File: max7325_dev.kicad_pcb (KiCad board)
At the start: 2 copper layers, 0 parts

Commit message: pcb: Place components on PCB
1. Export NET file from schematic editor
2. Import NET file in PCB editor

Signed-off-by: Sam Protsenko <joe.skb7@gmail.com>
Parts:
- added C1: 0.1uF, Capacitors_SMD:C_1206, F.Cu at (111.8, 35.6)
- added D0: LED, LEDs:LED_D5.0mm, F.Cu at (148.6, 83.8)
- added D1: LED, LEDs:LED_D5.0mm, F.Cu at (156.2, 83.8)
- added D10: LED, LEDs:LED_D5.0mm, F.Cu at (163.8, 72.4)
- added D11: LED, LEDs:LED_D5.0mm, F.Cu at (171.4, 72.4)
- added D12: LED, LEDs:LED_D5.0mm, F.Cu at (179.1, 72.4)
- added D13: LED, LEDs:LED_D5.0mm, F.Cu at (186.7, 72.4)
- added D14: LED, LEDs:LED_D5.0mm, F.Cu at (194.3, 72.4)
- added D15: LED, LEDs:LED_D5.0mm, F.Cu at (201.9, 72.4)
- added D2: LED, LEDs:LED_D5.0mm, F.Cu at (163.8, 83.8)
- added D3: LED, LEDs:LED_D5.0mm, F.Cu at (171.4, 83.8)
- added D4: LED, LEDs:LED_D5.0mm, F.Cu at (179.1, 83.8)
- added D5: LED, LEDs:LED_D5.0mm, F.Cu at (186.7, 83.8)
- added D6: LED, LEDs:LED_D5.0mm, F.Cu at (194.3, 83.8)
- added D7: LED, LEDs:LED_D5.0mm, F.Cu at (201.9, 83.8)
- added D8: LED, LEDs:LED_D5.0mm, F.Cu at (148.6, 72.4)
- added D9: LED, LEDs:LED_D5.0mm, F.Cu at (156.2, 72.4)
- added J1: Conn_01x06, Pin_Headers:Pin_Header_Straight_1x06_Pitch2.54mm, F.Cu at (105.4, 47.0)
- added JP0: Jumper_NC_Dual, Pin_Headers:Pin_Header_Straight_1x03_Pitch2.54mm, F.Cu at (179.1, 102.9)
- added JP1: Jumper_NC_Dual, Pin_Headers:Pin_Header_Straight_1x03_Pitch2.54mm, F.Cu at (190.5, 102.9)
- added JP2: Jumper_NC_Dual, Pin_Headers:Pin_Header_Straight_1x03_Pitch2.54mm, F.Cu at (203.2, 102.9)
- added JP3: Jumper_NC_Dual, Pin_Headers:Pin_Header_Straight_1x03_Pitch2.54mm, F.Cu at (215.9, 102.9)
- added JP4: Jumper_NC_Dual, Pin_Headers:Pin_Header_Straight_1x03_Pitch2.54mm, F.Cu at (228.6, 102.9)
- added JP5: Jumper_NC_Dual, Pin_Headers:Pin_Header_Straight_1x03_Pitch2.54mm, F.Cu at (242.6, 102.9)
- added JP6: Jumper_NC_Dual, Pin_Headers:Pin_Header_Straight_1x03_Pitch2.54mm, F.Cu at (256.5, 102.9)
- added JP7: Jumper_NC_Dual, Pin_Headers:Pin_Header_Straight_1x03_Pitch2.54mm, F.Cu at (271.8, 102.9)
- added MK1: Mounting_Hole_PAD, Mounting_Holes:MountingHole_3.2mm_M3_Pad, F.Cu at (115.6, 130.8)
- added MK2: Mounting_Hole_PAD, Mounting_Holes:MountingHole_3.2mm_M3_Pad, F.Cu at (128.3, 130.8)
- added MK3: Mounting_Hole_PAD, Mounting_Holes:MountingHole_3.2mm_M3_Pad, F.Cu at (143.5, 130.8)
- added MK4: Mounting_Hole_PAD, Mounting_Holes:MountingHole_3.2mm_M3_Pad, F.Cu at (158.8, 130.8)
- added R0: 220R, Resistors_SMD:R_1206, F.Cu at (135.9, 76.2)
- added R1: 220R, Resistors_SMD:R_1206, F.Cu at (135.9, 69.8)
- added R10: 220R, Resistors_SMD:R_1206, F.Cu at (128.3, 57.1)
- added R11: 220R, Resistors_SMD:R_1206, F.Cu at (128.3, 50.8)
- added R12: 220R, Resistors_SMD:R_1206, F.Cu at (128.3, 45.7)
- added R13: 220R, Resistors_SMD:R_1206, F.Cu at (128.3, 40.6)
- added R14: 220R, Resistors_SMD:R_1206, F.Cu at (128.3, 35.6)
- added R15: 220R, Resistors_SMD:R_1206, F.Cu at (120.7, 35.6)
- added R16: 10k, Resistors_SMD:R_1206, F.Cu at (120.7, 40.6)
- added R17: 10k, Resistors_SMD:R_1206, F.Cu at (120.7, 45.7)
- added R18: 0R, Resistors_SMD:R_1206, F.Cu at (120.7, 50.8)
- added R19: 0R, Resistors_SMD:R_1206, F.Cu at (120.7, 57.1)
- added R2: 220R, Resistors_SMD:R_1206, F.Cu at (135.9, 63.5)
- added R20: 0R, Resistors_SMD:R_1206, F.Cu at (120.7, 63.5)
- added R21: 0R, Resistors_SMD:R_1206, F.Cu at (120.7, 69.8)
- added R22: 10k, Resistors_SMD:R_1206, F.Cu at (120.7, 76.2)
- added R23: 10k, Resistors_SMD:R_1206, F.Cu at (120.7, 81.3)
- added R24: 10k, Resistors_SMD:R_1206, F.Cu at (120.7, 87.6)
- added R25: 10k, Resistors_SMD:R_1206, F.Cu at (120.7, 94.0)
- added R26: 10k, Resistors_SMD:R_1206, F.Cu at (120.7, 99.1)
- added R27: 10k, Resistors_SMD:R_1206, F.Cu at (120.7, 104.1)
- added R28: 10k, Resistors_SMD:R_1206, F.Cu at (120.7, 109.2)
- added R29: 10k, Resistors_SMD:R_1206, F.Cu at (120.7, 114.3)
- added R3: 220R, Resistors_SMD:R_1206, F.Cu at (135.9, 57.1)
- added R4: 220R, Resistors_SMD:R_1206, F.Cu at (135.9, 50.8)
- added R5: 220R, Resistors_SMD:R_1206, F.Cu at (135.9, 45.7)
- added R6: 220R, Resistors_SMD:R_1206, F.Cu at (135.9, 40.6)
- added R7: 220R, Resistors_SMD:R_1206, F.Cu at (135.9, 35.6)
- added R8: 220R, Resistors_SMD:R_1206, F.Cu at (128.3, 69.8)
- added R9: 220R, Resistors_SMD:R_1206, F.Cu at (128.3, 63.5)
- added SW0: SW_Push, Buttons_Switches_THT:SW_PUSH_6mm, F.Cu at (147.3, 57.1)
- added SW1: SW_Push, Buttons_Switches_THT:SW_PUSH_6mm, F.Cu at (158.8, 57.1)
- added SW2: SW_Push, Buttons_Switches_THT:SW_PUSH_6mm, F.Cu at (170.2, 57.1)
- added SW3: SW_Push, Buttons_Switches_THT:SW_PUSH_6mm, F.Cu at (181.6, 57.1)
- added SW4: SW_Push, Buttons_Switches_THT:SW_PUSH_6mm, F.Cu at (193.0, 57.1)
- added SW5: SW_Push, Buttons_Switches_THT:SW_PUSH_6mm, F.Cu at (204.5, 57.1)
- added SW6: SW_Push, Buttons_Switches_THT:SW_PUSH_6mm, F.Cu at (215.9, 57.1)
- added SW7: SW_Push, Buttons_Switches_THT:SW_PUSH_6mm, F.Cu at (227.3, 57.1)
- added U1: MAX7325AEG+, Housings_SSOP:QSOP-24_3.9x8.7mm_Pitch0.635mm, F.Cu at (105.4, 74.9)

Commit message: pcb: Finish PCB layout
Signed-off-by: Sam Protsenko <joe.skb7@gmail.com>
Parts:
- removed R22, R23, R24, R25, R26, R27, R28, R29: 10k, Resistors_SMD:R_1206
- added R100: 10k, Resistors_SMD:R_1206, B.Cu at (110.5, 80.0)
- added R101: 10k, Resistors_SMD:R_1206, B.Cu at (100.3, 80.0)
- added R102: 10k, Resistors_SMD:R_1206, B.Cu at (90.2, 80.0)
- added R103: 10k, Resistors_SMD:R_1206, B.Cu at (80.0, 80.0)
- added R104: 10k, Resistors_SMD:R_1206, B.Cu at (69.8, 80.0)
- added R105: 10k, Resistors_SMD:R_1206, B.Cu at (59.7, 80.0)
- added R106: 10k, Resistors_SMD:R_1206, B.Cu at (49.5, 80.0)
- added R107: 10k, Resistors_SMD:R_1206, B.Cu at (39.4, 80.0)
- C1, R0, R1, R10, R11, R12, R13, R14, R15, R16, R17, R18, R19, R2, R20, R21, R3, R4, R5, R6, R7, R8, R9, U1: moved to B.Cu
- moved JP7 236.6 mm to (36.8, 74.9), turned to 90 degrees
- moved JP6 211.4 mm to (47.0, 74.9), turned to 90 degrees
- moved SW7 194.0 mm to (36.8, 94.0)
- moved JP5 187.5 mm to (57.1, 74.9), turned to 90 degrees
- moved SW6 172.9 mm to (47.0, 94.0)
- moved JP4 163.7 mm to (67.3, 74.9), turned to 90 degrees
- moved D7 162.6 mm to (39.4, 85.1), turned to 270 degrees
- moved SW5 151.9 mm to (57.1, 94.0)
- moved D6 144.8 mm to (49.5, 85.1), turned to 270 degrees
- moved JP3 141.2 mm to (77.5, 74.9), turned to 90 degrees
- moved MK1 133.3 mm to (29.2, 29.2)
- moved SW4 131.0 mm to (67.3, 94.0)
- moved D5 127.0 mm to (59.7, 85.1), turned to 270 degrees
- moved JP2 118.9 mm to (87.6, 74.9), turned to 90 degrees
- moved MK3 118.0 mm to (29.2, 101.6)
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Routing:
- net +3V3: track 0.00 -> 533.7 mm, vias 0 -> 2
- net GND: track 0.00 -> 231.0 mm
- net Net-(R19-Pad2): track 0.00 -> 52.4 mm
- net /RST: track 0.00 -> 50.8 mm
- net Net-(R18-Pad2): track 0.00 -> 47.3 mm
- net /P0: track 0.00 -> 45.8 mm
- net /INT: track 0.00 -> 45.5 mm
- net /P7: track 0.00 -> 44.6 mm
- net /SCL: track 0.00 -> 44.2 mm
- net /O8: track 0.00 -> 44.1 mm
- net /O15: track 0.00 -> 43.1 mm
- net /SDA: track 0.00 -> 42.2 mm
- net /P1: track 0.00 -> 35.9 mm
- net /O9: track 0.00 -> 35.4 mm
- net /P6: track 0.00 -> 34.7 mm
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- added copper zone on B.Cu, net GND
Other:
- board outline added: 100.3 x 80 mm
- net class Default: clearance 0.2 -> 0.2032; trace_width 0.25 -> 0.254; via_dia 0.6 -> 1.2; via_drill 0.4 -> 0.8
- net class Medium added: clearance 0.2032, trace_width 0.381, via_dia 2, via_drill 0.8
- rule trace_clearance: 0.2 -> 0.2032
- rule trace_min: 0.2 -> 0.254
- rule via_min_size: 0.4 -> 0.8

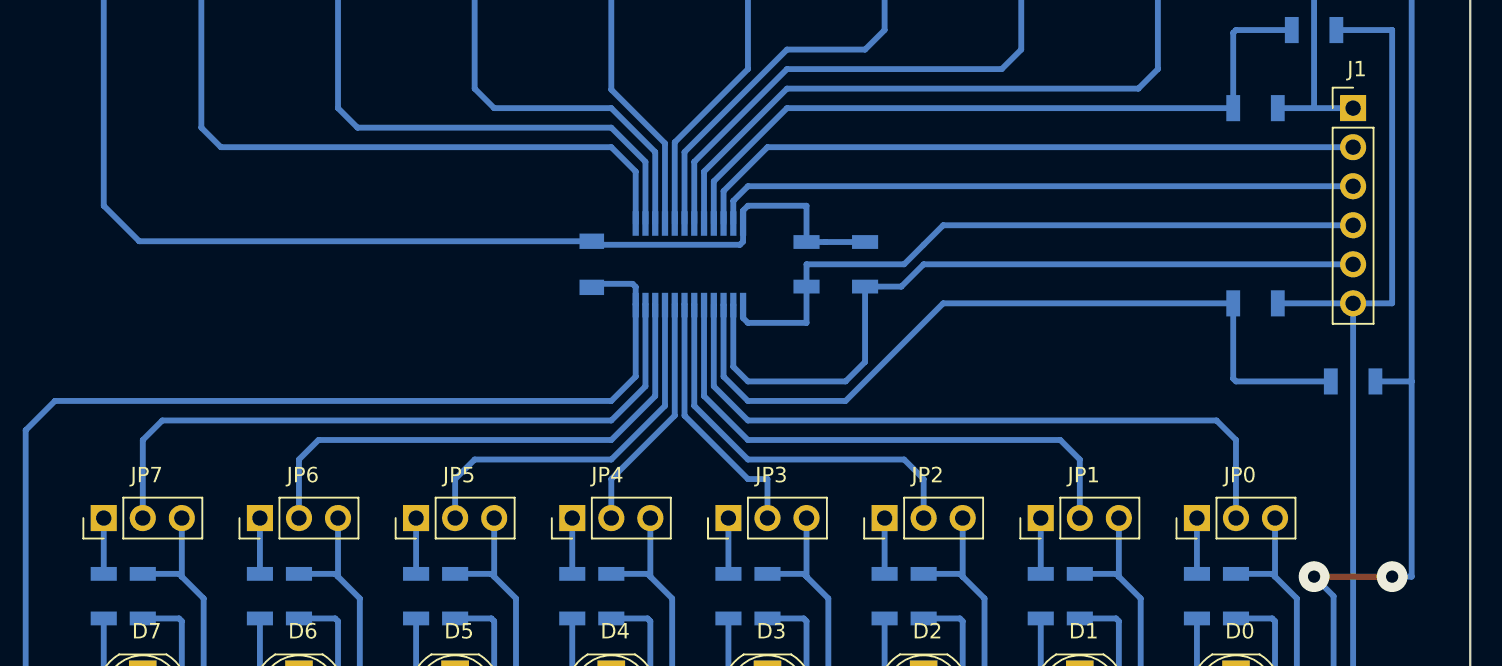
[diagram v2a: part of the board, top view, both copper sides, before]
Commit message: pcb: Add silk text for header pins
Signed-off-by: Sam Protsenko <joe.skb7@gmail.com>
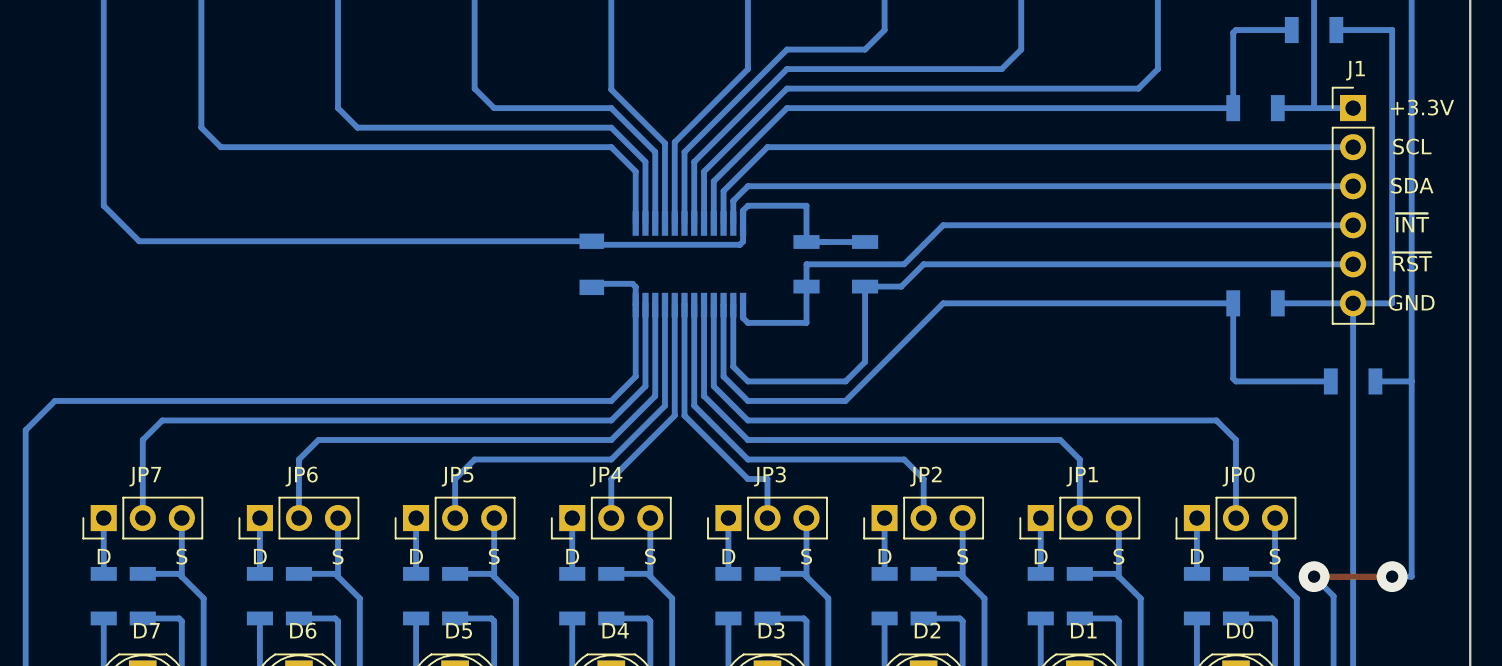
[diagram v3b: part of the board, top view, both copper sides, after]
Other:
- board text added: "+3.3V"
- board text added: "D"
- board text added: "GND"
- board text added: "S"
- board text added: "SCL"
- board text added: "SDA"
- board text added: "~INT"
- board text added: "~RST"
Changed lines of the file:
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@@
     (links 128)
     (no_connects 0)
-    (area 21.792514 24.0318 129.337487 106.8782)
+    (area 25.324999 25.324999 125.805001 105.485001)
     (thickness 1.6)
-    (drawings 4)
+    (drawings 26)
     (tracks 327)
     (zones 0)
@@
     (tags "resistor 1206")
     (attr smd)
-    (fp_text reference R100 (at 0 1.85 90) (layer B.SilkS)
+    (fp_text reference R100 (at -3.175 0 180) (layer B.SilkS)
       (effects (font (size 1 1) (thickness 0.15)) (justify mirror))
     )
@@
     (tags "resistor 1206")
     (attr smd)
-    (fp_text reference R101 (at 0 1.85 90) (layer B.SilkS)
+    (fp_text reference R101 (at -3.175 0 180) (layer B.SilkS)
       (effects (font (size 1 1) (thickness 0.15)) (justify mirror))
     )
@@
     (tags "resistor 1206")
     (attr smd)
-    (fp_text reference R102 (at 0 1.85 90) (layer B.SilkS)
+    (fp_text reference R102 (at -3.175 0 180) (layer B.SilkS)
       (effects (font (size 1 1) (thickness 0.15)) (justify mirror))
     )
@@
     (tags "resistor 1206")
     (attr smd)
-    (fp_text reference R103 (at 0 1.85 90) (layer B.SilkS)
+    (fp_text reference R103 (at -3.175 0 180) (layer B.SilkS)
       (effects (font (size 1 1) (thickness 0.15)) (justify mirror))
     )
@@
     (tags "resistor 1206")
     (attr smd)
-    (fp_text reference R104 (at 0 1.85 90) (layer B.SilkS)
+    (fp_text reference R104 (at -3.175 0 180) (layer B.SilkS)
       (effects (font (size 1 1) (thickness 0.15)) (justify mirror))
     )
@@
     (tags "resistor 1206")
     (attr smd)
-    (fp_text reference R105 (at 0 1.85 90) (layer B.SilkS)
+    (fp_text reference R105 (at -3.175 0 180) (layer B.SilkS)
       (effects (font (size 1 1) (thickness 0.15)) (justify mirror))
     )
@@
     (tags "resistor 1206")
     (attr smd)
-    (fp_text reference R106 (at 0 1.85 90) (layer B.SilkS)
+    (fp_text reference R106 (at -3.175 0 180) (layer B.SilkS)
       (effects (font (size 1 1) (thickness 0.15)) (justify mirror))
     )
@@
     (tags "resistor 1206")
     (attr smd)
-    (fp_text reference R107 (at 0 1.85 90) (layer B.SilkS)
+    (fp_text reference R107 (at -3.175 0 180) (layer B.SilkS)
       (effects (font (size 1 1) (thickness 0.15)) (justify mirror))
     )
@@
       (rotate (xyz 0 0 0))
     )
+  )
+  (gr_line (start 25.4 25.4) (end 125.73 25.4) (angle 90) (layer Edge.Cuts) (width 0.15))
+  (gr_text S (at 113.03 77.47) (layer F.SilkS)
+    (effects (font (size 1 1) (thickness 0.15)))
+  )
+  (gr_text D (at 107.95 77.47) (layer F.SilkS)
+    (effects (font (size 1 1) (thickness 0.15)))
+  )
+  (gr_text S (at 102.87 77.47) (layer F.SilkS)
+    (effects (font (size 1 1) (thickness 0.15)))
+  )
+  (gr_text D (at 97.79 77.47) (layer F.SilkS)
+    (effects (font (size 1 1) (thickness 0.15)))
+  )
+  (gr_text S (at 92.71 77.47) (layer F.SilkS)
+    (effects (font (size 1 1) (thickness 0.15)))
+  )
+  (gr_text D (at 87.63 77.47) (layer F.SilkS)
+    (effects (font (size 1 1) (thickness 0.15)))
+  )
+  (gr_text S (at 82.55 77.47) (layer F.SilkS)
+    (effects (font (size 1 1) (thickness 0.15)))
+  )
+  (gr_text D (at 77.47 77.47) (layer F.SilkS)
+    (effects (font (size 1 1) (thickness 0.15)))
+  )
+  (gr_text S (at 72.39 77.47) (layer F.SilkS)
+    (effects (font (size 1 1) (thickness 0.15)))
+  )
+  (gr_text D (at 67.31 77.47) (layer F.SilkS)
+    (effects (font (size 1 1) (thickness 0.15)))
+  )
+  (gr_text S (at 62.23 77.47) (layer F.SilkS)
+    (effects (font (size 1 1) (thickness 0.15)))
+  )
+  (gr_text D (at 57.15 77.47) (layer F.SilkS)
+    (effects (font (size 1 1) (thickness 0.15)))
+  )
+  (gr_text S (at 52.07 77.47) (layer F.SilkS)
+    (effects (font (size 1 1) (thickness 0.15)))
+  )
+  (gr_text D (at 46.99 77.47) (layer F.SilkS)
+    (effects (font (size 1 1) (thickness 0.15)))
+  )
+  (gr_text S (at 41.91 77.47) (layer F.SilkS)
+    (effects (font (size 1 1) (thickness 0.15)))
+  )
+  (gr_text D (at 36.83 77.47) (layer F.SilkS)
+    (effects (font (size 1 1) (thickness 0.15)))
+  )
+  (gr_text GND (at 121.92 60.96) (layer F.SilkS)
+    (effects (font (size 1 1) (thickness 0.15)))
+  )
+  (gr_text ~RST (at 121.92 58.42) (layer F.SilkS)
+    (effects (font (size 1 1) (thickness 0.15)))
+  )
+  (gr_text ~INT (at 121.92 55.88) (layer F.SilkS)
+    (effects (font (size 1 1) (thickness 0.15)))
+  )
+  (gr_text SDA (at 121.92 53.34) (layer F.SilkS)
+    (effects (font (size 1 1) (thickness 0.15)))
+  )
+  (gr_text SCL (at 121.92 50.8) (layer F.SilkS)
+    (effects (font (size 1 1) (thickness 0.15)))
+  )
+  (gr_text +3.3V (at 122.555 48.26) (layer F.SilkS)
+    (effects (font (size 1 1) (thickness 0.15)))
   )
   (gr_line (start 25.4 105.41) (end 25.4 25.4) (angle 90) (layer Edge.Cuts) (width 0.15))
   (gr_line (start 125.73 105.41) (end 25.4 105.41) (angle 90) (layer Edge.Cuts) (width 0.15))
   (gr_line (start 125.73 25.4) (end 125.73 105.41) (angle 90) (layer Edge.Cuts) (width 0.15))
-  (gr_line (start 25.4 25.4) (end 125.73 25.4) (angle 90) (layer Edge.Cuts) (width 0.15))
   (segment (start 68.58 56.92) (end 39.14 56.92) (width 0.381) (layer B.Cu) (net 1))
   (segment (start 39.37 29.21) (end 43.18 29.21) (width 0.381) (layer B.Cu) (net 1))

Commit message: Migrate to KiCad 5.0
Signed-off-by: Sam Protsenko <joe.skb7@gmail.com>
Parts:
- C1: footprint Capacitors_SMD:C_1206 -> Capacitor_SMD:C_1206_3216Metric
- D0, D1, D10, D11, D12, D13, D14, D15, D2, D3, D4, D5, D6, D7, D8, D9: footprint LEDs:LED_D5.0mm -> LED_THT:LED_D5.0mm
- J1: footprint Pin_Headers:Pin_Header_Straight_1x06_Pitch2.54mm -> Connector_PinHeader_2.54mm:PinHeader_1x06_P2.54mm_Vertical
- JP0, JP1, JP2, JP3, JP4, JP5, JP6, JP7: footprint Pin_Headers:Pin_Header_Straight_1x03_Pitch2.54mm -> Connector_PinHeader_2.54mm:PinHeader_1x03_P2.54mm_Vertical
- MK1, MK2, MK3, MK4: footprint Mounting_Holes:MountingHole_3.2mm_M3_Pad -> MountingHole:MountingHole_3.2mm_M3_Pad
- R0, R1, R10, R100, R101, R102, R103, R104, R105, R106, R107, R11, R12, R13, R14, R15, R16, R17, R18, R19, R2, R20, R21, R3, R4, R5, R6, R7, R8, R9: footprint Resistors_SMD:R_1206 -> Resistor_SMD:R_1206_3216Metric
- SW0, SW1, SW2, SW3, SW4, SW5, SW6, SW7: footprint Buttons_Switches_THT:SW_PUSH_6mm -> Button_Switch_THT:SW_PUSH_6mm
- U1: footprint Housings_SSOP:QSOP-24_3.9x8.7mm_Pitch0.635mm -> Package_SO:QSOP-24_3.9x8.7mm_P0.635mm
